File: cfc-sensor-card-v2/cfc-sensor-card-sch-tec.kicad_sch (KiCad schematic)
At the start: 19 parts, among them IC1 AD5593RBCPZ-RL7, U12 DRV8212DSGR, U14 MP2410A

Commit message: Update
updated opd address resistors to 100 ohms from 100 ohms, changed the 100 ohm res VBUSP to 10 ohms. Updated TEC page for sensor to have bidirectional current sense for diag. Removed misc testpoints
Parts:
- removed IC1: AD5593RBCPZ-RL7, oresat-ics:16-WFQFN, CSP, symbol oresat-ics:AD5593RBCPZ-RL7
- added C71: .022uF, oresat-passives:0603-C-NOSILK, symbol Device:C_Small
- added C72: 100n, oresat-passives:0603-C-NOSILK, symbol Device:C_Small
- added D5: GREEN, LED_SMD:LED_0603_1608Metric, symbol Device:LED_Small
- added D6: AMBER, LED_SMD:LED_0603_1608Metric, symbol Device:LED_Small
- added R57: 4.7K, oresat-passives:0603-C-NOSILK, symbol Device:R_Small_US
- added R60, R66, R67: 10K, oresat-passives:0603-C-NOSILK, symbol Device:R_Small_US
- added R68: 25m, Resistor_SMD:R_2512_6332Metric, symbol Device:R_Small_US
- added R69, R70: 100, oresat-passives:0603-C-NOSILK, symbol Device:R_Small_US
- added U13: AD5593RBCPZ-RL7, oresat-ics:16-WFQFN, CSP, symbol oresat-ics:AD5593RBCPZ-RL7
- added U15: INA186A1IDCKR, oresat-ics:SOIC_IDCKR_TEX, symbol oresat-ics:INA186A1IDCKR
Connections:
- net 2.5VREF: now also R60.1, U13.6 (VREF)
- net 3.3V: now also C72.1, U13.1 (VDD), U13.15 (~{RESET}), U13.7 (VLOGIC), U15.3 (VS)
- net BRIDGE_EN: now also U13.3 (I/O1)
- net CURRENT_SET: now also U13.2 (I/O0)
- net GND: now also C72.2, D5.1 (K), D6.1 (K), R67.2, U13.12 (GND), U15.2 (GND)
- net I2C1_CLK: now also U13.14 (SCL)
- net I2C1_SDA: now also U13.13 (SDA)
- net TEC_OUT2: now also R68.2, R70.1; no longer U12.3 (OUT2)
- net THERM+: now also U13.11 (I/O7)
- net at R58.2: now also U13.16 (A0)
- net BRIDGE_PHASE renamed BRIDGE_DIR
- net BRIDGE_DIR: now also U13.4 (I/O2)
- new net: R60.2, R67.1, U15.1 (REF)
- new net: D6.2 (A), R57.2
- new net: D5.2 (A), R66.1
- new net: R68.1, R69.1, U12.3 (OUT2)
- new net: C71.2, R69.2, U15.4 (IN+)
- new net: C71.1, R70.2, U15.5 (IN-)
- new net TEC_SENSE: U13.5 (I/O3), U15.6 (OUT)
- no-connect marks 4 -> 3
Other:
- note added: ""COOL""
- note added: ""TEC""
- note added: ".0495*25=1.2375v .0505v*25=1.2625v"
- note added: "0805"
- note added: "2512"
- note added: "25v/v gain"
- note added: "Bulk cap may need to change depending on output current"
- note added: "Change bottom to 19k and 400 ohm split divider"
- note added: "Max 2a output V=2*.025±1% =.0495-.0505v .0505v*2a =.191watts"
- note added: "Needs an AND gate"
- note added: "Needs an OR gate"
- note removed: "Bulk cap may need to change depending current output"
- note removed: "This circuit is way more efficient but more complicated."
- moved on the sheet: C69

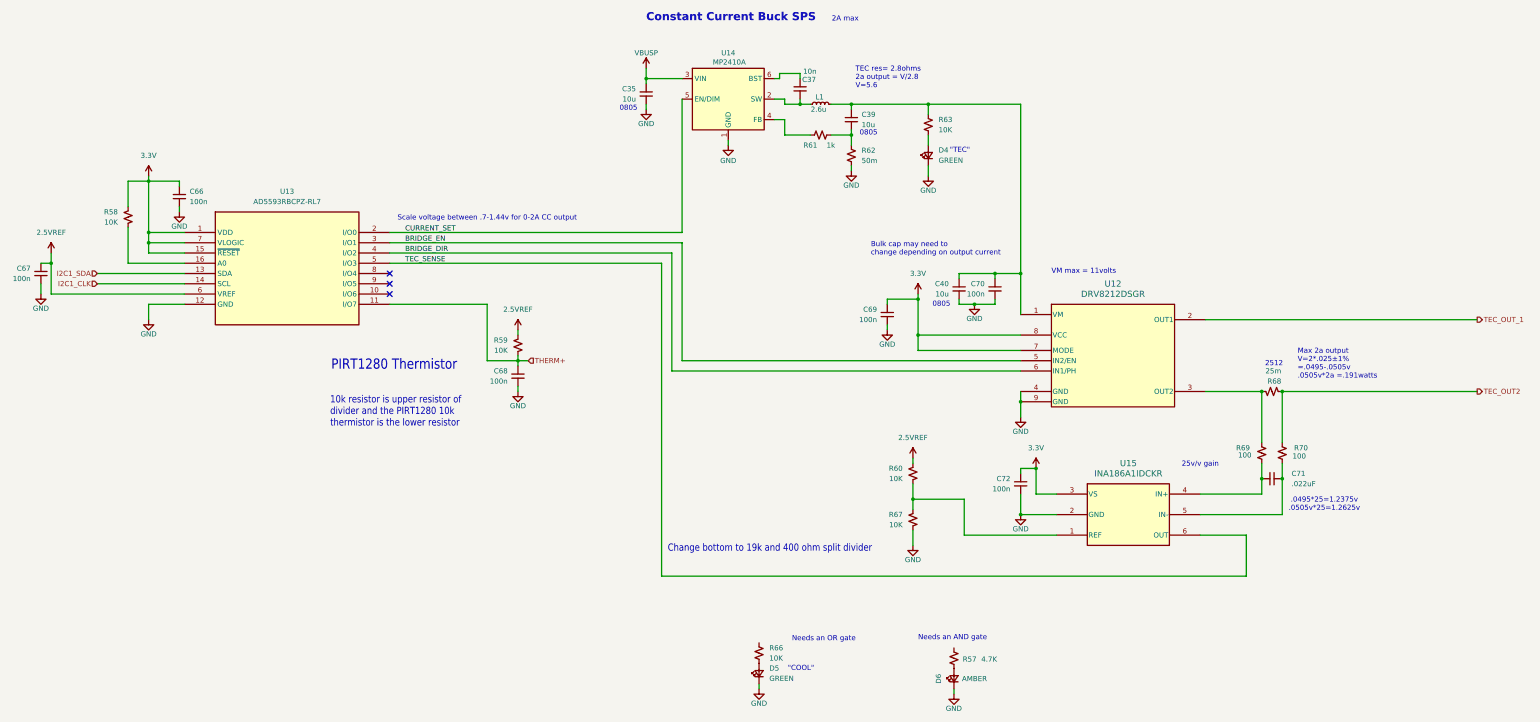
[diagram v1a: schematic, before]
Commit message: Update
added logic gates to heating and cooling led indicators.
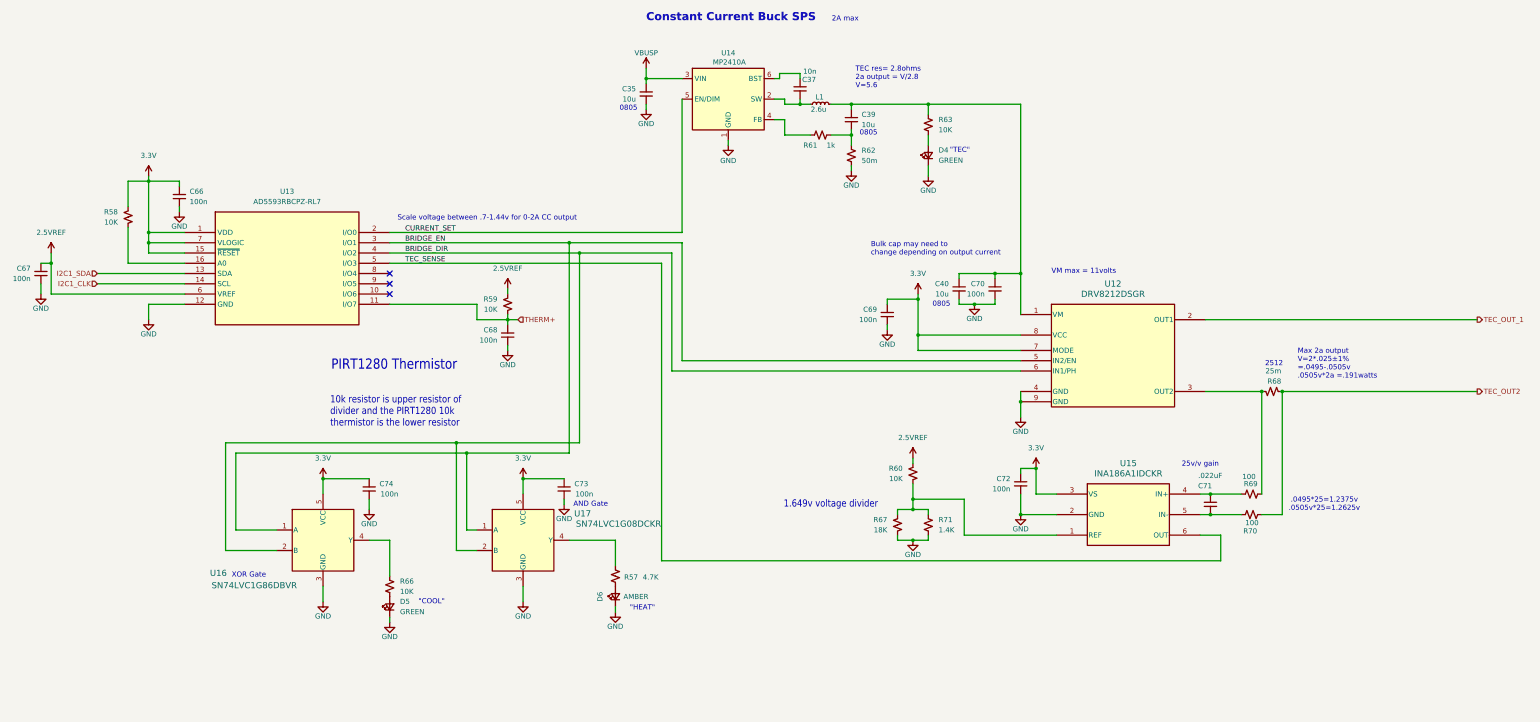
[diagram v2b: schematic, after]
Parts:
- added C73, C74: 100n, oresat-passives:0603-C-NOSILK, symbol Device:C_Small
- added R71: 1.4K, oresat-passives:0603-C-NOSILK, symbol Device:R_Small_US
- added U16: SN74LVC1G86DBVR, oresat-ics:DBV5, symbol oresat-ics:SN74LVC1G86DBVR
- added U17: SN74LVC1G08DCKR, oresat-ics:DCK5-L, symbol oresat-ics:SN74LVC1G08DCKR
- R67: value 10K -> 18K; DPN 708-RNCF0603TKW10K0 -> 71-TNPW060318K0BYCN; MFR Stackpole Electronics Inc -> Vishay; MPN RNCF0603TKW10K0 -> TNPW060318K0BYCN
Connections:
- net 3.3V: now also C73.1, C74.1, U16.5 (VCC), U17.5 (VCC)
- net BRIDGE_DIR: now also U16.2 (B), U17.2 (B)
- net BRIDGE_EN: now also U16.1 (A), U17.1 (A)
- net GND: now also C73.2, C74.2, R71.2, U16.3 (GND), U17.3 (GND)
- net TEC_OUT2: now also R70.2; no longer R70.1
- net at R60.2, R67.1, U15.1 (REF): now also R71.1
- net at R57.1: now also U17.4 (Y)
- net at R66.2: now also U16.4 (Y)
- net at R68.1, U12.3 (OUT2): now also R69.2; no longer R69.1
- new net: C71.1, R69.1, U15.4 (IN+)
- new net: C71.2, R70.1, U15.5 (IN-)
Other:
- note added: ""HEAT""
- note added: "1.649v voltage divider"
- note added: "AND Gate"
- note added: "XOR Gate"
- note removed: "Change bottom to 19k and 400 ohm split divider"
- note removed: "Needs an AND gate"
- note removed: "Needs an OR gate"
- moved on the sheet: C68, C71, D5, D6, R57, R59, R66, R67
